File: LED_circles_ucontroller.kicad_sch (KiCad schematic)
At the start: 19 parts, among them J1 Conn_ARM_SWD_TagConnect_TC203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, U3 STM32F070CBTx, U75 M95256-WMN6P, U76 M95256-WMN6P

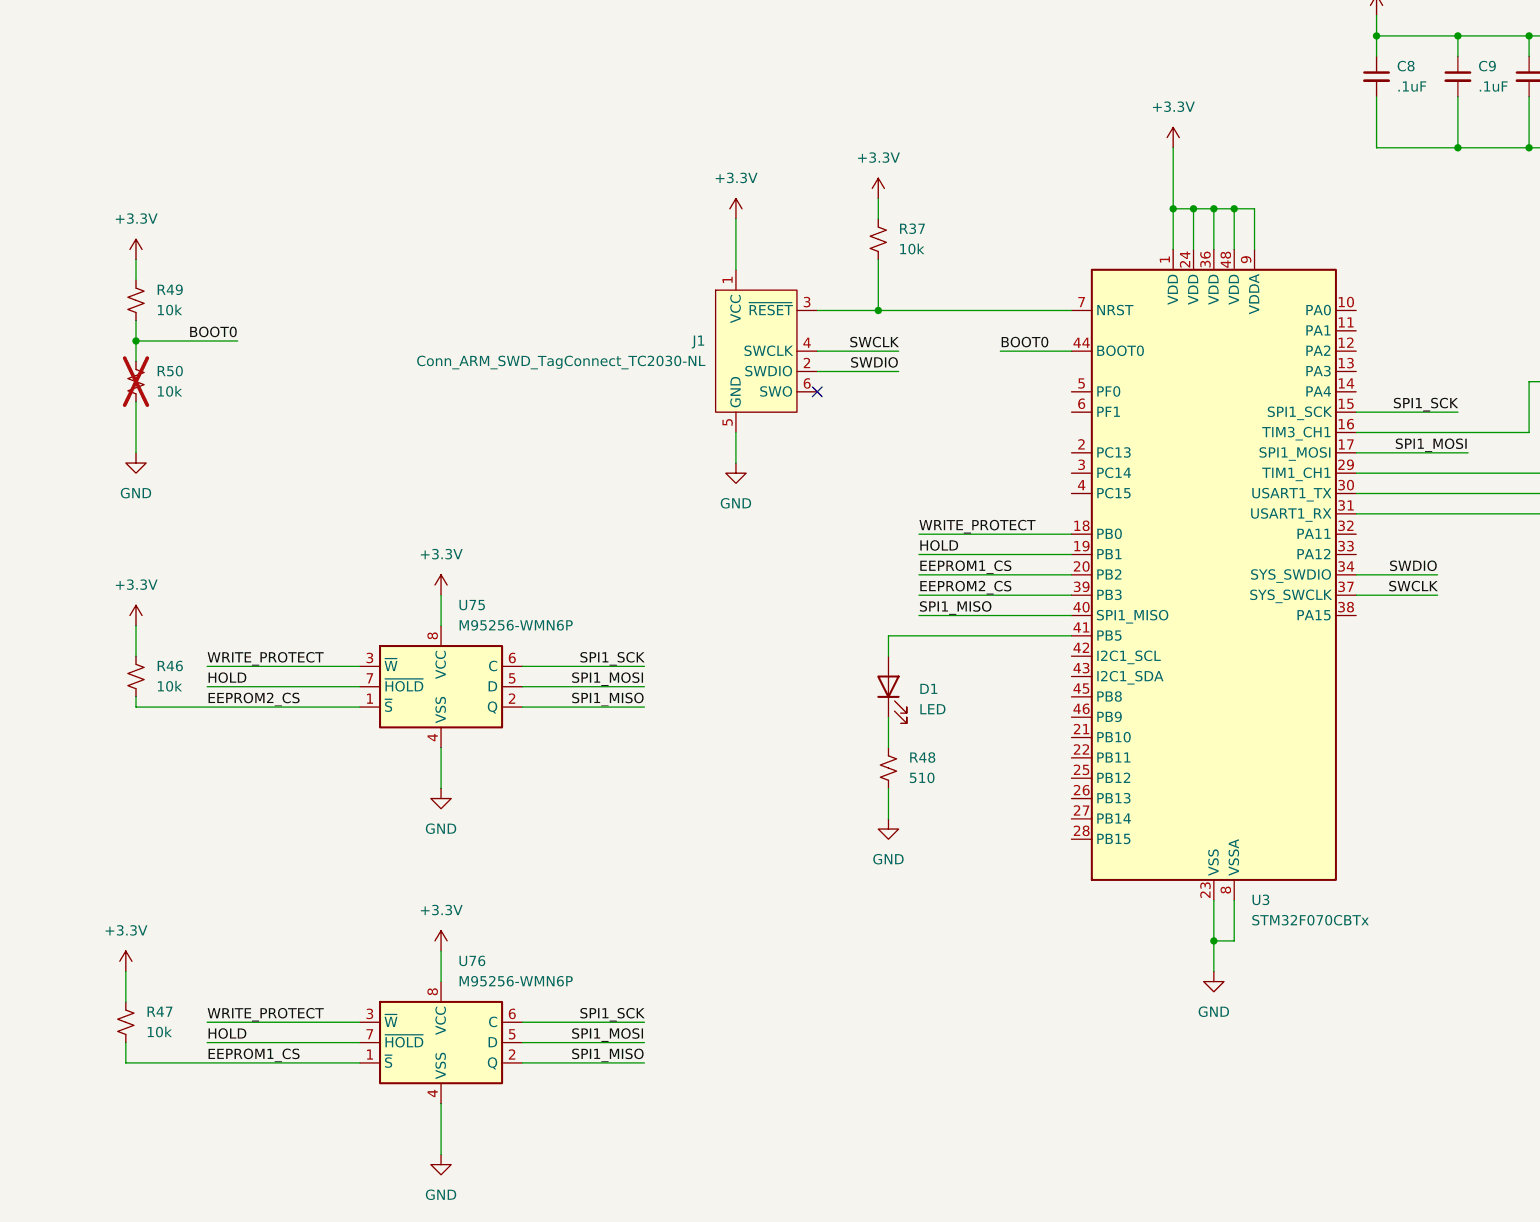
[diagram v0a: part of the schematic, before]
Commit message: Initial layout of top layer
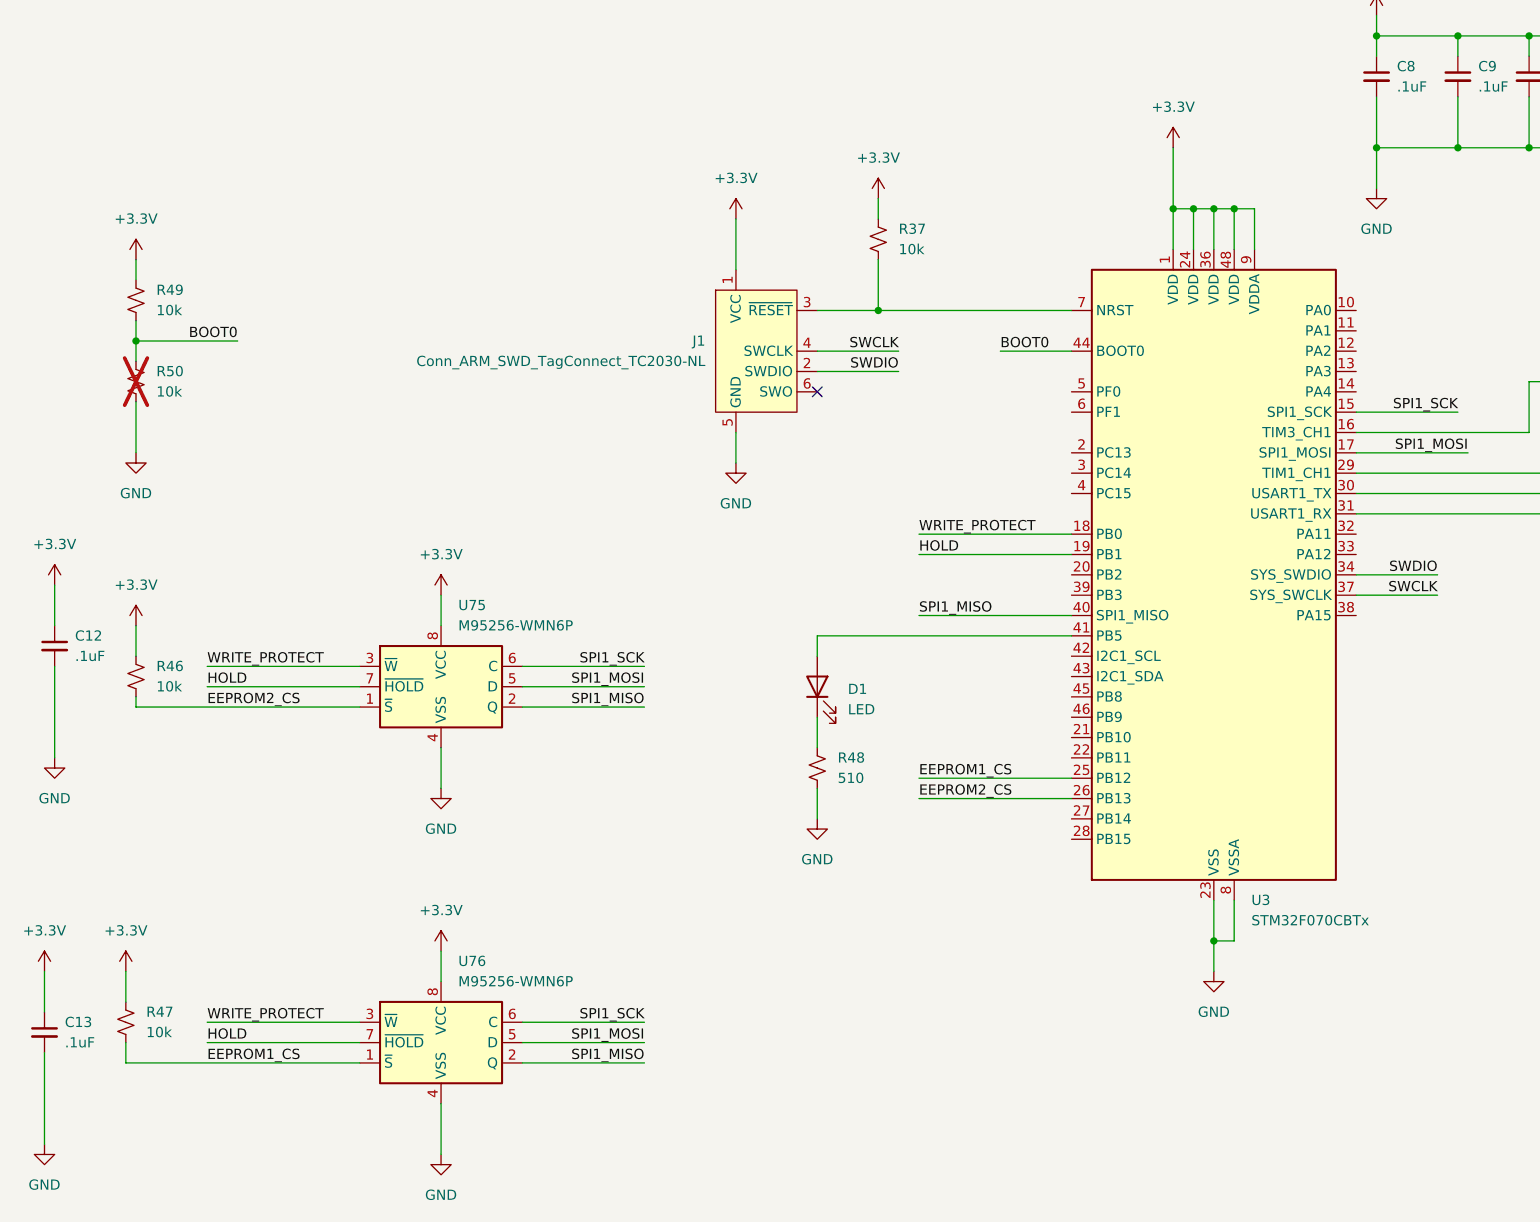
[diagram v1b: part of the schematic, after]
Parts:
- added C12, C13: .1uF, Capacitor_SMD:C_0805_2012Metric, symbol Device:C_Small
- TP1, TP2: footprint TestPoint:TestPoint_Keystone_5005-5009_Compact -> TestPoint:TestPoint_Pad_3.0x3.0mm
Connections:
- net +3.3V: now also C12.1, C13.1
- net EEPROM1_CS: now also U3.25 (PB12); no longer U3.20 (PB2)
- net EEPROM2_CS: now also U3.26 (PB13); no longer U3.39 (PB3)
- net GND: now also C10.2, C11.2, C8.2, C9.2, C12.2, C13.2
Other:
- moved on the sheet: D1, R48

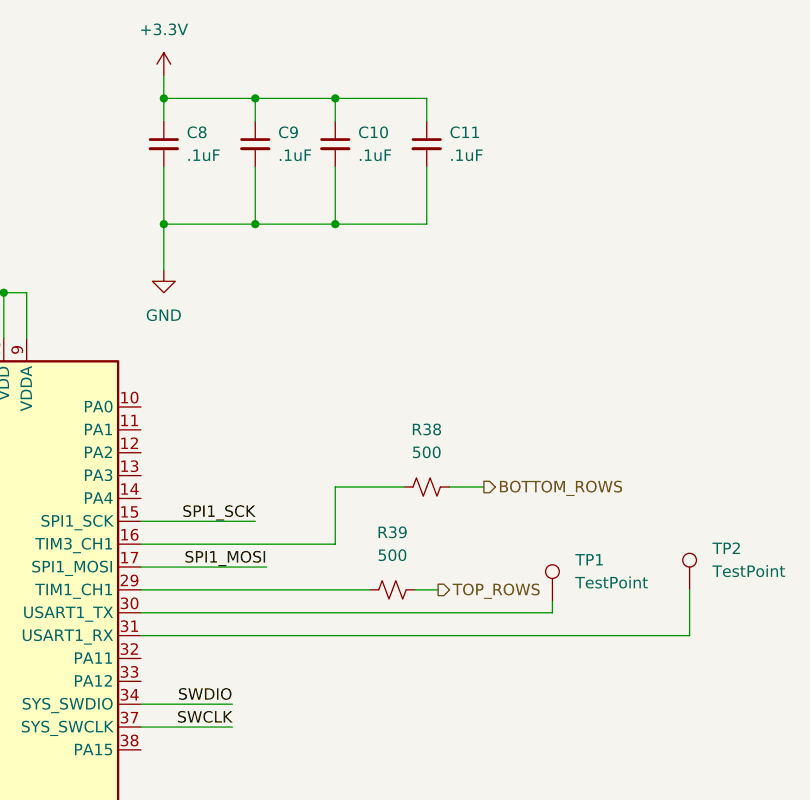
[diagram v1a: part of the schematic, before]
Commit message: Fixed PCB DRC issues.
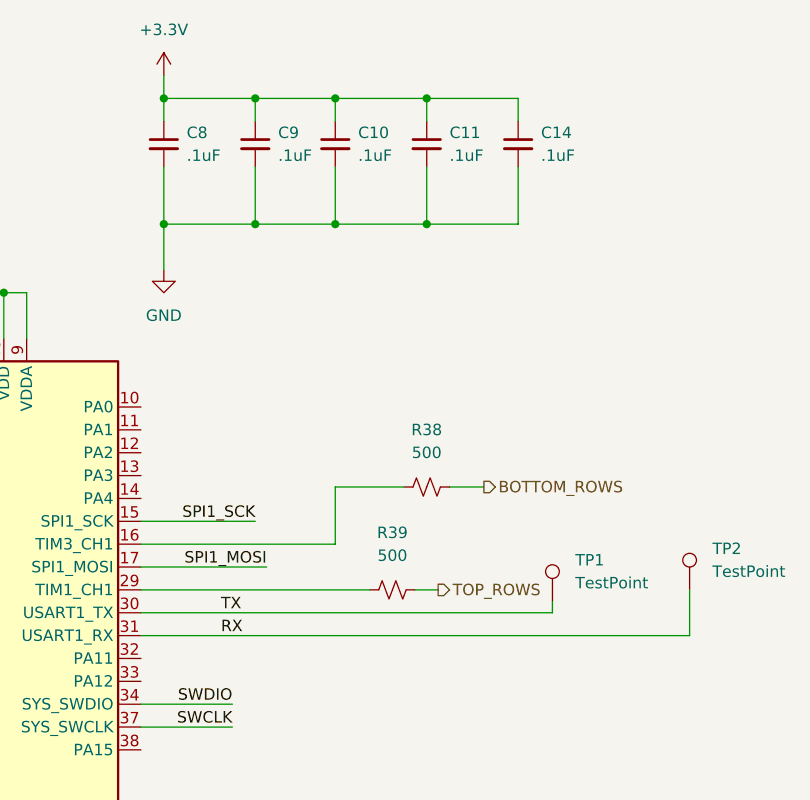
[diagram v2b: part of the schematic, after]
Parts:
- added C14: .1uF, Capacitor_SMD:C_0805_2012Metric, symbol Device:C_Small
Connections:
- net +3.3V: now also C14.1
- net GND: now also C14.2
- net RX: now reaches TP2.1, U3.31 (PA10)
- net TX: now reaches TP1.1, U3.30 (PA9)
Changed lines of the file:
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@@
+	)
+	(junction
+		(at 285.75 35.56)
+		(diameter 0)
+		(color 0 0 0 0)
 	)
 	(junction
@@
 	)
 	(junction
+		(at 285.75 49.53)
+		(diameter 0)
+		(color 0 0 0 0)
+	)
+	(junction
 		(at 275.59 35.56)
 		(diameter 0)
@@
 	(wire
 		(pts
+			(xy 285.75 35.56) (xy 295.91 35.56)
+		)
+		(stroke
+			(width 0)
+			(type default)
+		)
+	)
+	(wire
+		(pts
 			(xy 256.54 49.53) (xy 256.54 54.61)
 		)
@@
 	(wire
 		(pts
+			(xy 295.91 35.56) (xy 295.91 38.1)
+		)
+		(stroke
+			(width 0)
+			(type default)
+		)
+	)
+	(wire
+		(pts
 			(xy 149.86 161.29) (xy 165.1 161.29)
 		)
@@
 	(wire
 		(pts
+			(xy 295.91 43.18) (xy 295.91 49.53)
+		)
+		(stroke
+			(width 0)
+			(type default)
+		)
+	)
+	(wire
+		(pts
 			(xy 101.6 119.38) (xy 129.54 119.38)
 		)
@@
 		(pts
 			(xy 100.33 152.4) (xy 100.33 156.21)
+		)
+		(stroke
+			(width 0)
+			(type default)
+		)
+	)
+	(wire
+		(pts
+			(xy 285.75 49.53) (xy 295.91 49.53)
 		)
 		(stroke
@@
 		)
 	)
+	(label "RX"
+		(at 262.89 95.25 0)
+		(effects
+			(font
+				(size 1.27 1.27)
+			)
+			(justify left bottom)
+		)
+	)
 	(label "SWDIO"
 		(at 264.16 102.87 180)
@@
 			)
 			(justify right bottom)
+		)
+	)
+	(label "TX"
+		(at 262.89 92.71 0)
+		(effects
+			(font
+				(size 1.27 1.27)
+			)
+			(justify left bottom)
 		)
 	)
@@
 					(unit 1)
 				)
+			)
+		)
+	)
+	(symbol
+		(lib_id "Device:C_Small")
+		(at 295.91 40.64 0)
+		(unit 1)
+		(exclude_from_sim no)
+		(in_bom yes)
+		(on_board yes)
+		(dnp no)
+		(fields_autoplaced yes)
+		(property "Reference" "C14"
+			(at 298.45 39.3762 0)
+			(effects
+				(font
+					(size 1.27 1.27)
+				)
+				(justify left)
+			)
+		)
+		(property "Value" ".1uF"
+			(at 298.45 41.9162 0)
+			(effects
+				(font
+					(size 1.27 1.27)
+				)
+				(justify left)
+			)
+		)
+		(property "Footprint" "Capacitor_SMD:C_0805_2012Metric"
+			(at 295.91 40.64 0)
+			(effects
+				(font
+					(size 1.27 1.27)
+				)
+				(hide yes)
+			)
+		)
+		(property "Datasheet" "~"
+			(at 295.91 40.64 0)
+			(effects
+				(font
+					(size 1.27 1.27)
+				)
+				(hide yes)
+			)
+		)
+		(property "Description" "Unpolarized capacitor, small symbol"
+			(at 295.91 40.64 0)
+			(effects
+				(font
+					(size 1.27 1.27)
+				)
+				(hide yes)
+			)
+		)
+		(pin "2"
+		)
+		(pin "1"
+		)
+		(instances
+			(project "LED_circles"
+				(path "/fee5cc62-df5b-4e25-a1c9-d9673ac3b8e2/a02ddc3d-cba5-487a-854d-aeab8652491a"
+					(reference "C14")
+					(unit 1)
+				)

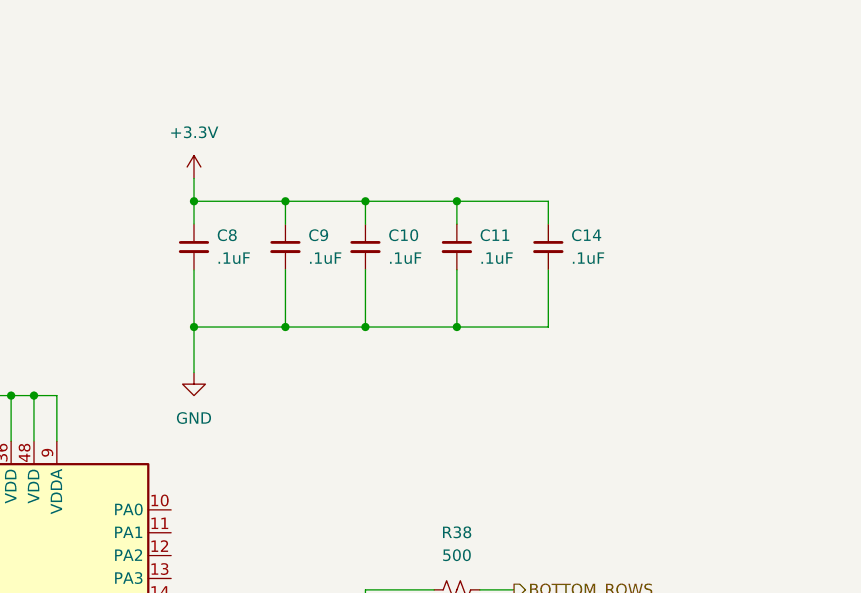
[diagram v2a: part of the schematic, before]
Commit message: Removed unnecessary jumper resistor
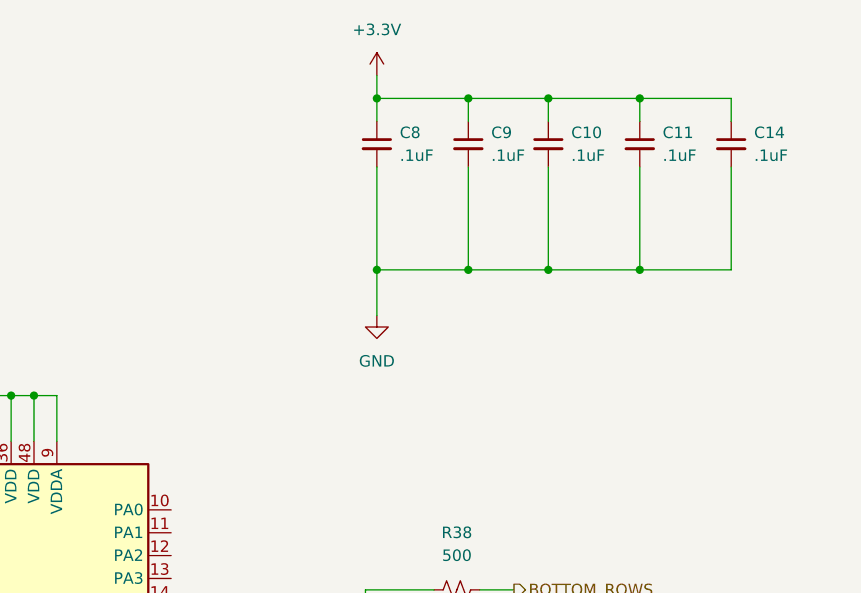
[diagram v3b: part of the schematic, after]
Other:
- moved on the sheet: C10, C11, C14, C8, C9

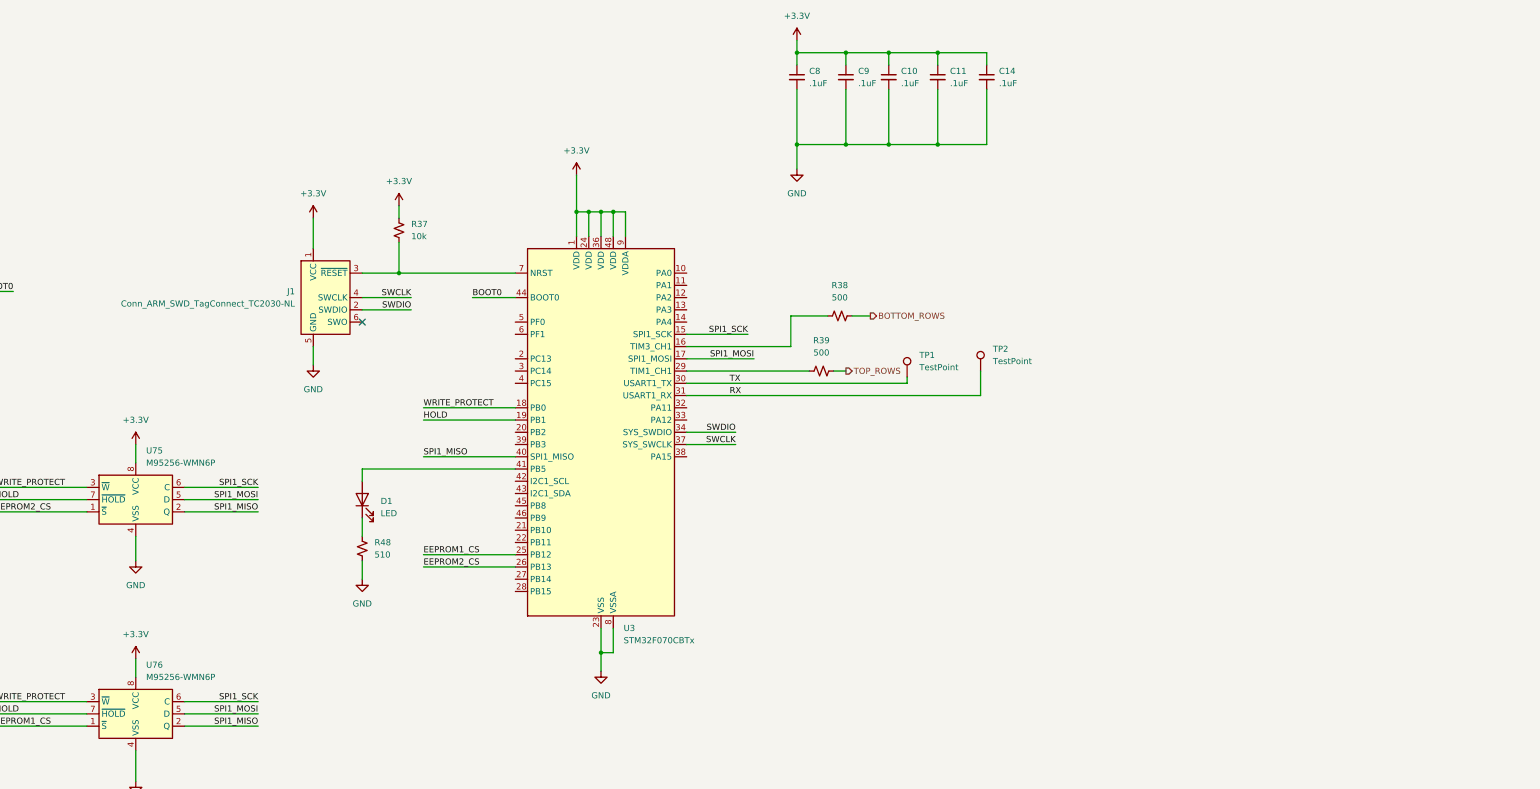
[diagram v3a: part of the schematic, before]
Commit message: Changed micro controller to larger package
- Also changed PCB DRC to work with OSH Park
- Changed SWD connection to generic  0.1" pogopin headers
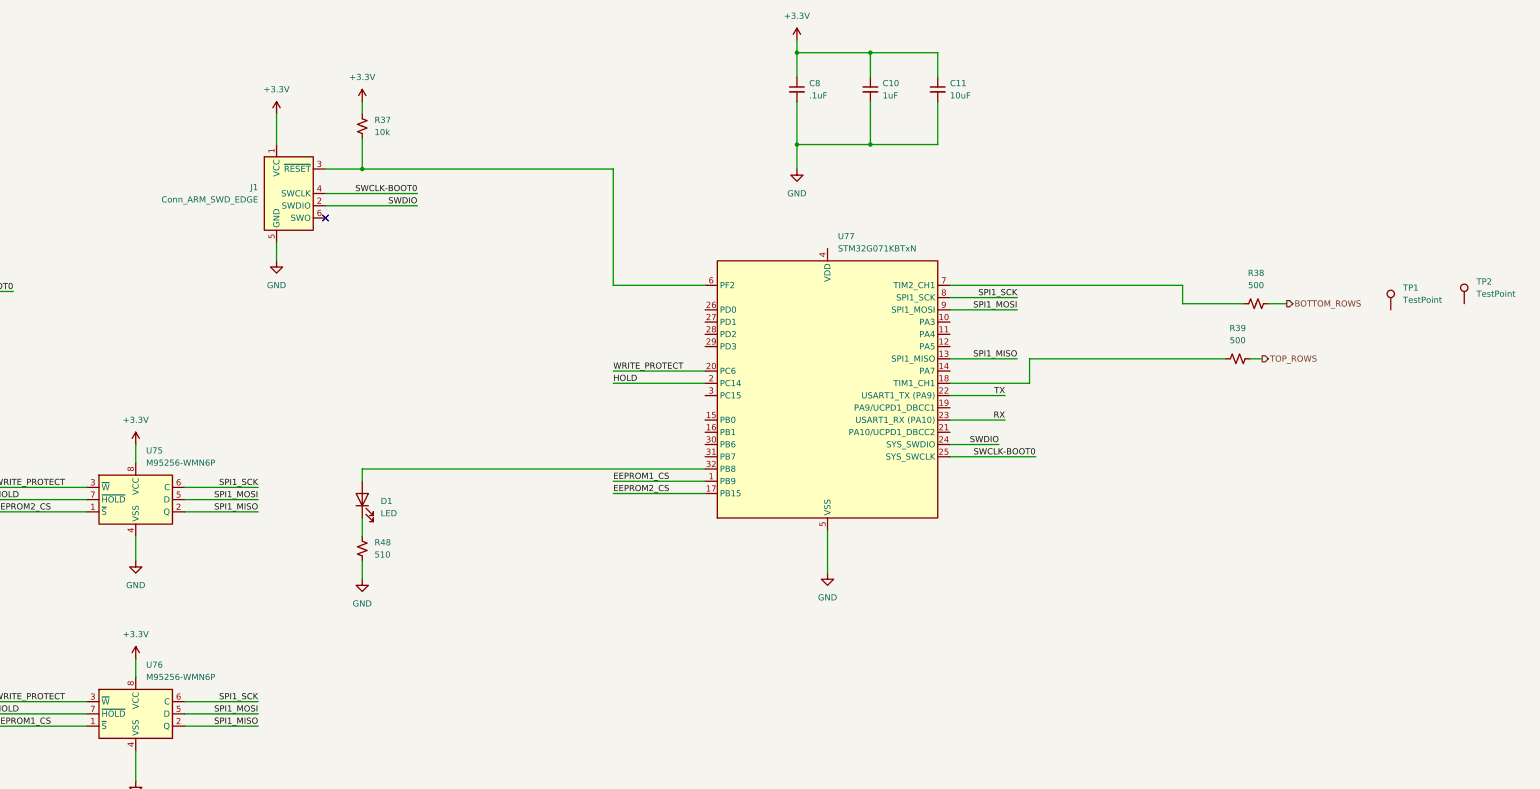
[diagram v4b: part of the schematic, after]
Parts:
- removed C14, C9: .1uF, Capacitor_SMD:C_0805_2012Metric, symbol Device:C_Small
- removed U3: STM32F070CBTx, Package_QFP:LQFP-48_7x7mm_P0.5mm, symbol MCU_ST_STM32F0:STM32F070CBTx
- added U77: STM32G071KBTxN, Package_QFP:LQFP-32_7x7mm_P0.8mm, symbol MCU_ST_STM32G0:STM32G071KBTxN
- C10: value .1uF -> 1uF
- C11: value .1uF -> 10uF
- J1: value Conn_ARM_SWD_TagConnect_TC2030-NL -> Conn_ARM_SWD_EDGE; footprint Connector:Tag-Connect_TC2030-IDC-NL_2x03_P1.27mm_Vertical -> LED_circles_footprints:ARM_SWD_EDGE; symbol Connector:Conn_ARM_SWD_TagConnect_TC2030-NL -> LED_circles_library:Conn_ARM_SWD_EDGE
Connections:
- net EEPROM1_CS: now also U77.1 (PB9)
- net EEPROM2_CS: now also U77.17 (PB15)
- net GND: now also U77.5 (VSS)
- net HOLD: now also U77.2 (PC14)
- net RX: now also U77.23 (PA10/PA12); no longer TP2.1
- net SPI1_MISO: now also U77.13 (PA6)
- net SPI1_MOSI: now also U77.9 (PA2)
- net SPI1_SCK: now also U77.8 (PA1)
- net SWDIO: now also U77.24 (PA13)
- net TX: now also U77.22 (PA9/PA11); no longer TP1.1
- net WRITE_PROTECT: now also U77.20 (PC6)
- net at R38.1: now also U77.7 (PA0)
- net at J1.3 (~{RESET}), R37.2: now also U77.6 (PF2)
- net at R39.1: now also U77.18 (PA8)
- net at D1.2 (A): now also U77.32 (PB8)
- net SWCLK renamed SWCLK-BOOT0
- net SWCLK-BOOT0: now also U77.25 (PA14)
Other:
- moved on the sheet: C10, C11, C8, J1, R37, R38, R39, TP1, TP2
